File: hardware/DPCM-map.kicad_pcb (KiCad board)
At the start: 2 copper layers, 178 x 178 mm, 101 parts, among them J1 JMP, J2 Conn_01x06_Male, J3 Touch_Pad_+, J4 Touch_Pad_0, J5 Touch_Pad_-, J6 JMP, J7 Conn_01x06_Female, P1 USB_C_Plug, Q1 2N7002, Q2 2N7002, SW1 SW_Push, SW2 SW_+_Fb, SW3 SW_0_Fb, SW4 SW_-_Fb, U1 AZ1117-3.3, U2 BME280, U4 ESP32-WROOM-32, U5 CH340G, Y1 12MHz

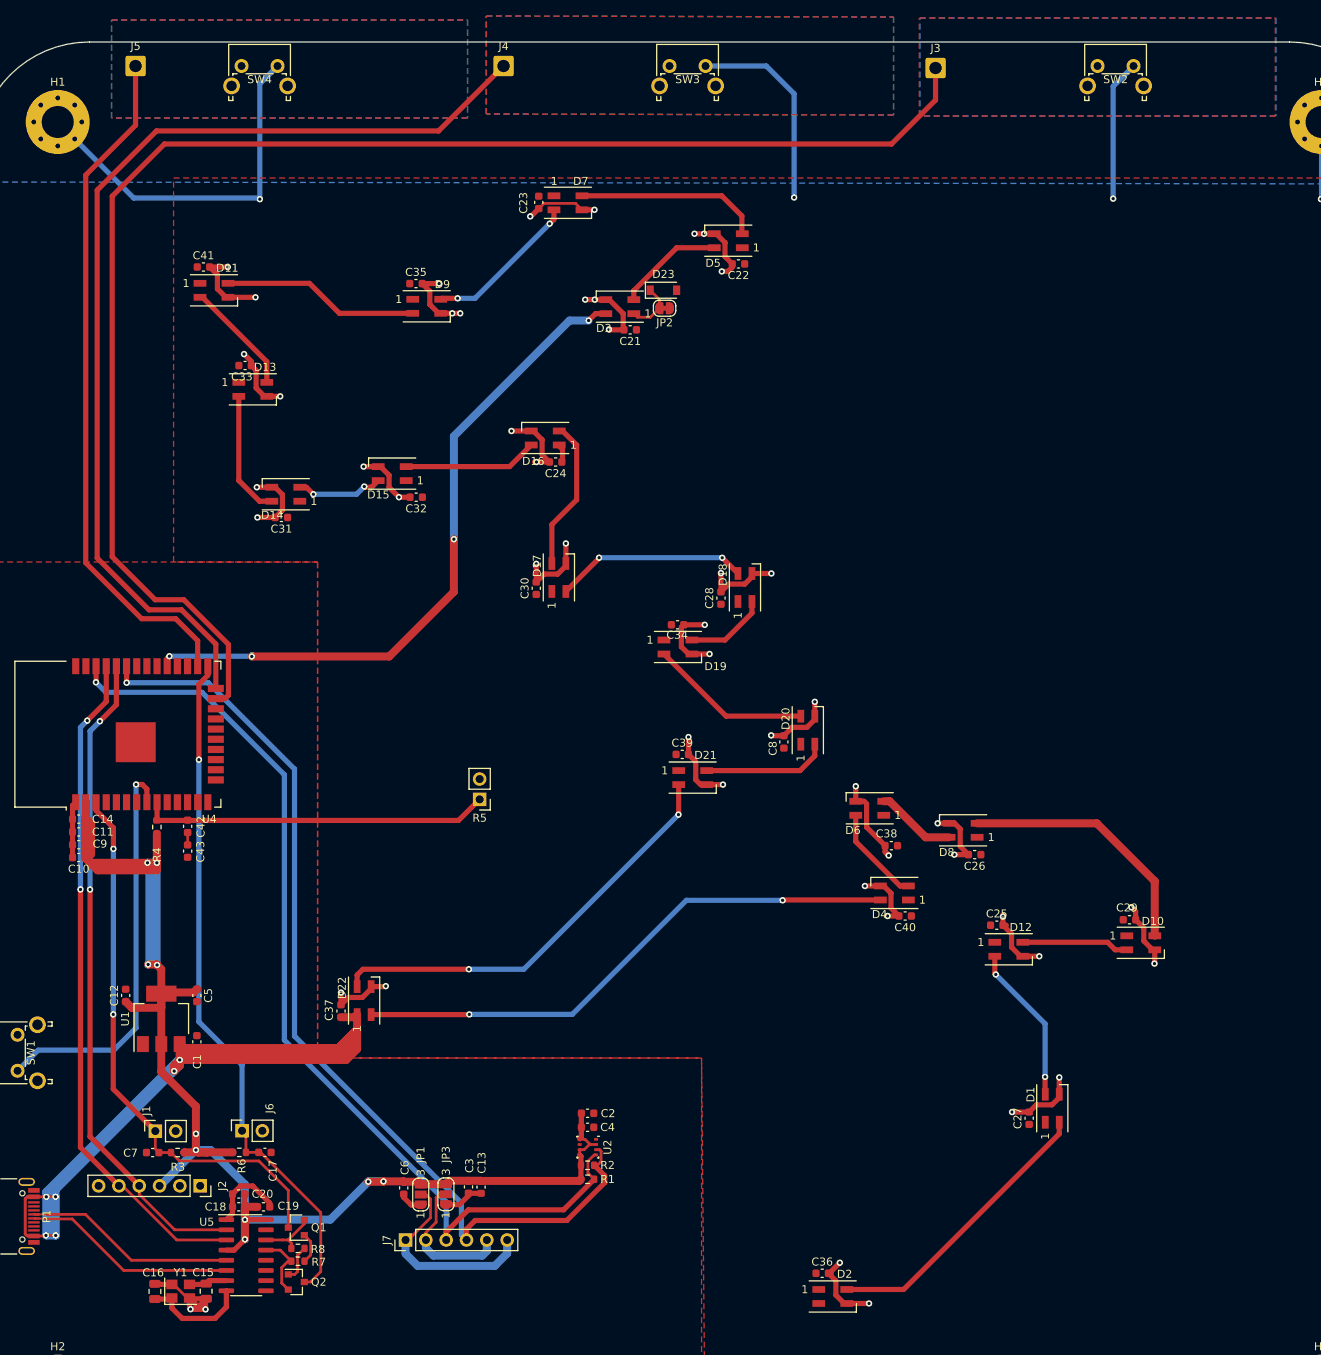
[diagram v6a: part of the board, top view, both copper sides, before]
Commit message: fix touchplates, optim traces and gnd fills
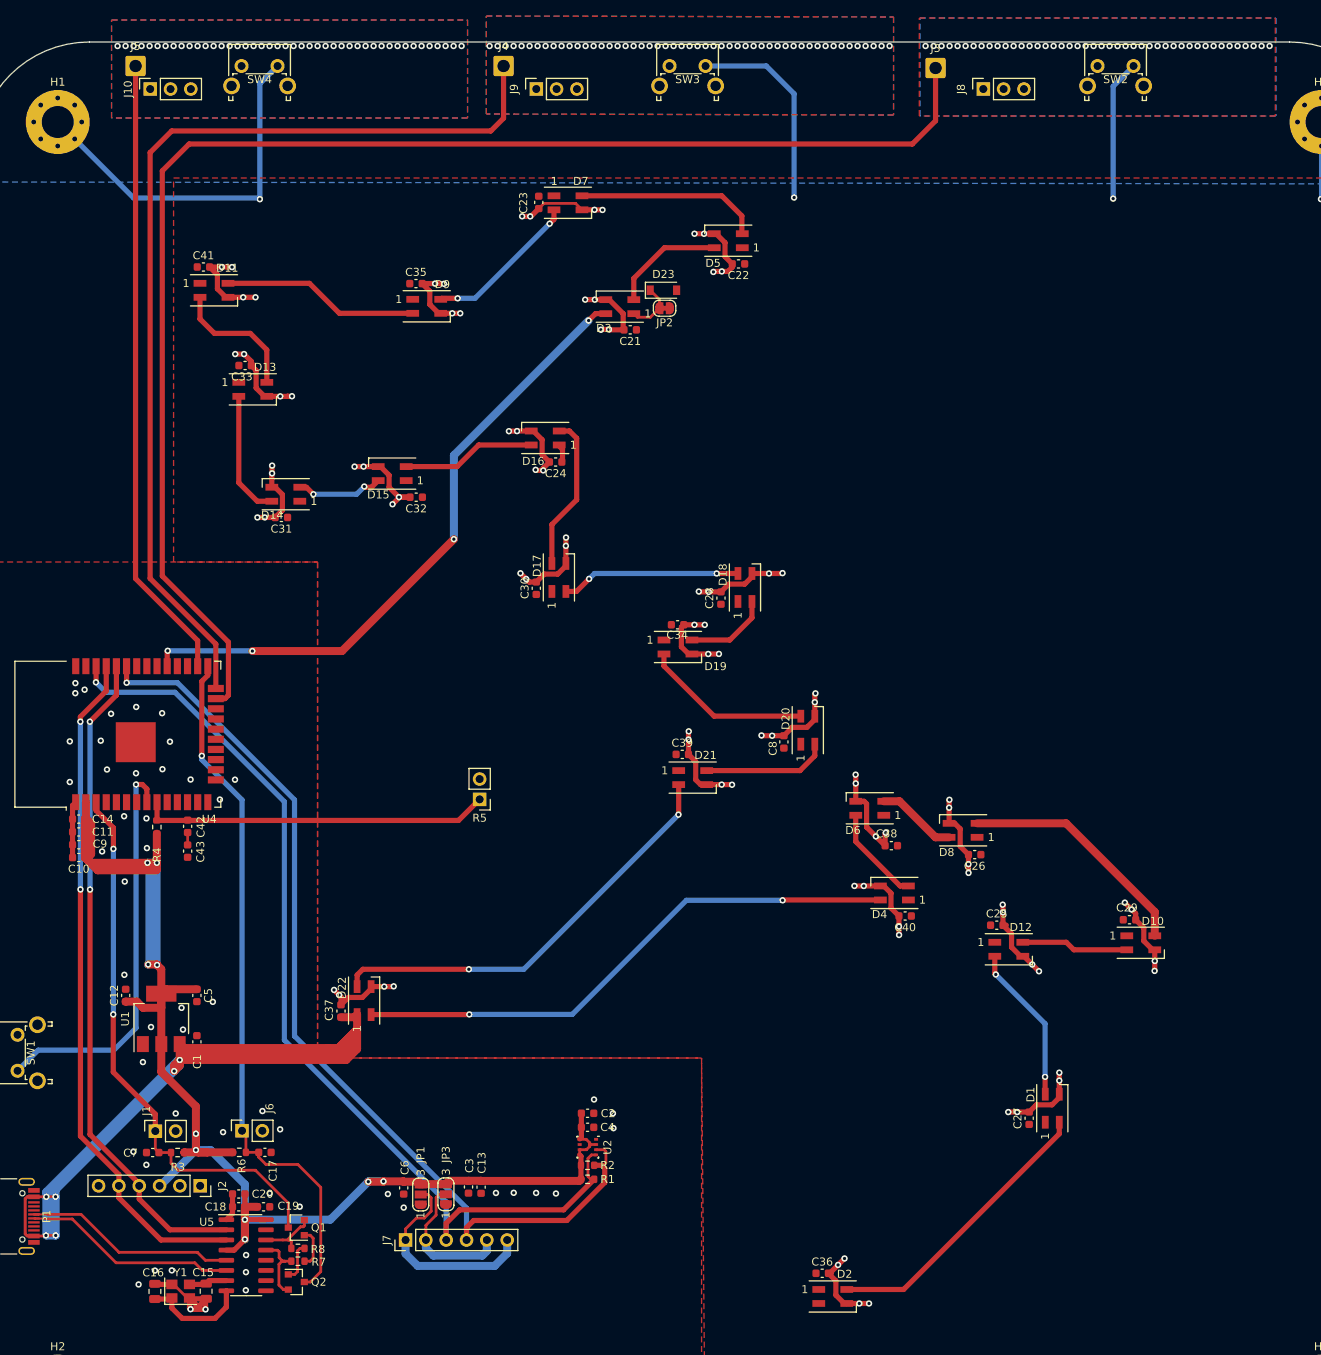
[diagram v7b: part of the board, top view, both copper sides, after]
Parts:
- added J10: Conn_01x03_Female, Connector_PinSocket_2.54mm:PinSocket_1x03_P2.54mm_Vertical, F.Cu at (132.1, 55.9)
- added J8: Conn_01x03_Female, Connector_PinSocket_2.54mm:PinSocket_1x03_P2.54mm_Vertical, F.Cu at (236.2, 55.9)
- added J9: Conn_01x03_Female, Connector_PinSocket_2.54mm:PinSocket_1x03_P2.54mm_Vertical, F.Cu at (180.3, 55.9)
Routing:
- net GND: track 348.5 -> 368.7 mm, vias 53 -> 144
- net TOUCH_-: track 85.9 -> 78.2 mm, vias 0 -> 44
- net TOUCH_+: track 184.1 -> 176.6 mm, vias 0 -> 44
- net TOUCH_0: track 128.0 -> 122.9 mm, vias 0 -> 51
- net LED_CHAIN: track 85.3 -> 80.3 mm
- net Net-(D11-Pad2): track 14.3 -> 16.7 mm
- net Net-(D10-Pad4): track 32.0 -> 29.8 mm
- net BOOT0: track 86.1 -> 88.0 mm
- net Net-(D17-Pad2): track 24.2 -> 22.4 mm
- net SDA: track 122.1 -> 120.8 mm
- net Net-(Q1-Pad1): track 3.90 -> 5.00 mm
- net Net-(D3-Pad2): track 13.4 -> 14.3 mm
- net TX: track 84.5 -> 85.4 mm
- net SCL: track 123.0 -> 122.2 mm
- net Net-(D19-Pad2): track 20.3 -> 21.2 mm
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
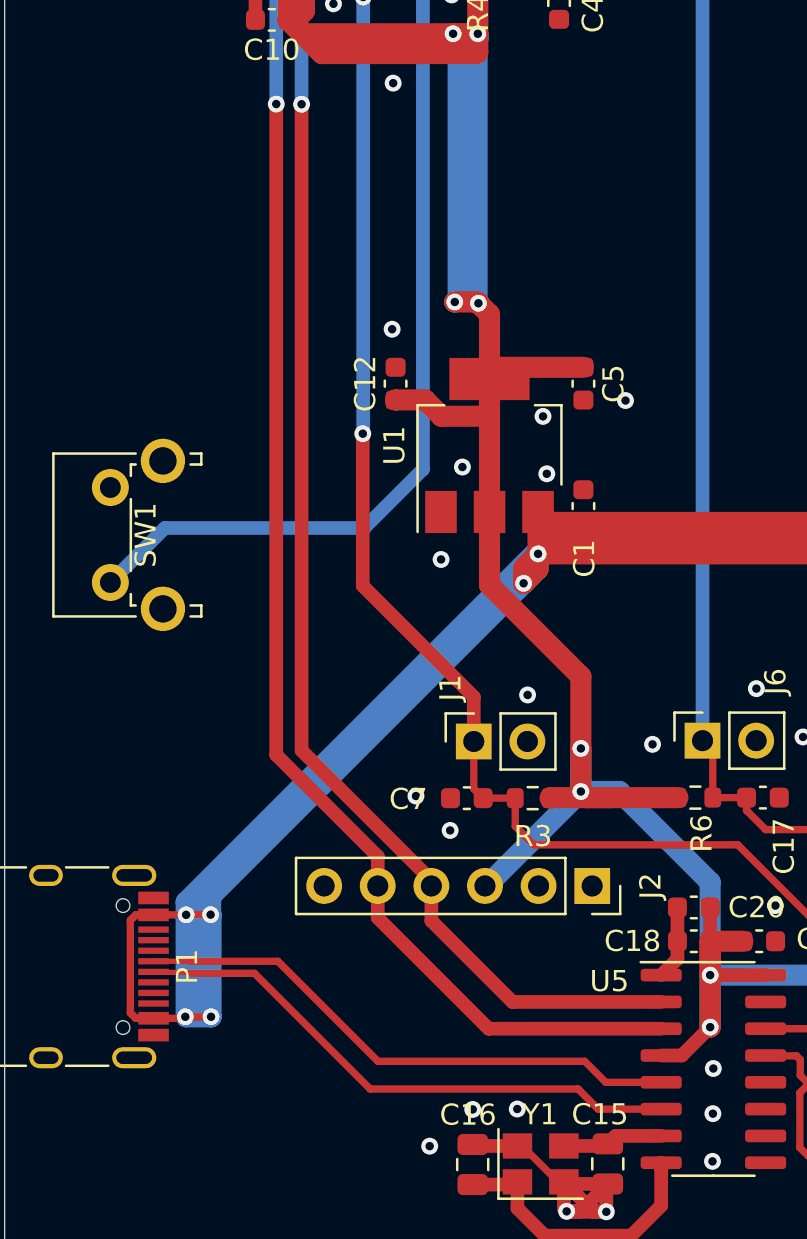
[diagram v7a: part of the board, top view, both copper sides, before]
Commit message: added heatsink for regulator
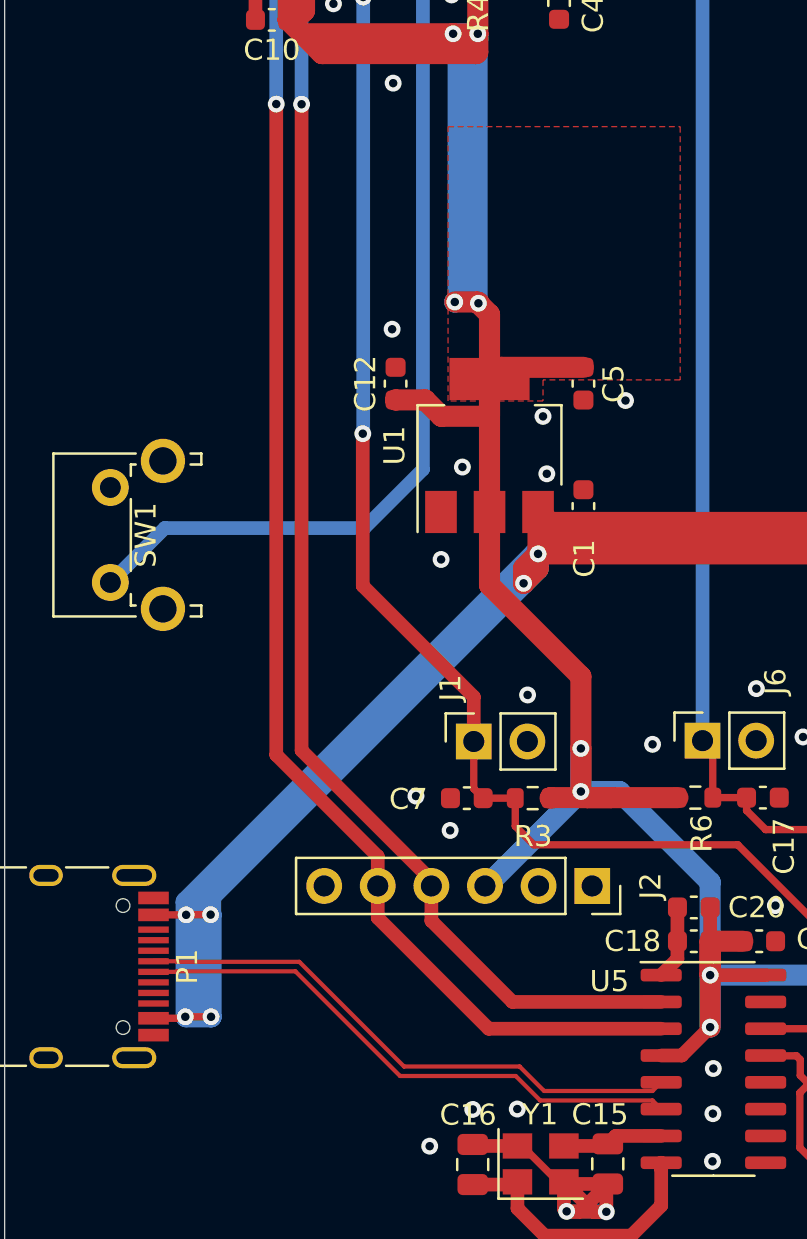
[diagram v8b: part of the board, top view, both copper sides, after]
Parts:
- C2: value 1u -> 10u
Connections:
- D2 pad 2: (no net) -> Net-(D2-Pad2)
- J2 pad 1: (no net) -> Net-(J2-Pad1)
- J2 pad 2: (no net) -> Net-(J2-Pad2)
- P1 pad A5: (no net) -> Net-(P1-PadA5)
- P1 pad A8: (no net) -> Net-(P1-PadA8)
- P1 pad B5: (no net) -> Net-(P1-PadB5)
- P1 pad B8: (no net) -> Net-(P1-PadB8)
- U4 pad 10: (no net) -> Net-(U4-Pad10)
- U4 pad 11: (no net) -> Net-(U4-Pad11)
- U4 pad 12: (no net) -> Net-(U4-Pad12)
- U4 pad 13: (no net) -> Net-(U4-Pad13)
- U4 pad 14: (no net) -> Net-(U4-Pad14)
- U4 pad 16: (no net) -> Net-(U4-Pad16)
- U4 pad 17: (no net) -> Net-(U4-Pad17)
- U4 pad 18: (no net) -> Net-(U4-Pad18)
- U4 pad 19: (no net) -> Net-(U4-Pad19)
- U4 pad 20: (no net) -> Net-(U4-Pad20)
- U4 pad 21: (no net) -> Net-(U4-Pad21)
- U4 pad 22: (no net) -> Net-(U4-Pad22)
- U4 pad 27: (no net) -> Net-(U4-Pad27)
- U4 pad 28: (no net) -> Net-(U4-Pad28)
- U4 pad 30: (no net) -> Net-(U4-Pad30)
- U4 pad 31: (no net) -> Net-(U4-Pad31)
- U4 pad 32: (no net) -> Net-(U4-Pad32)
- U4 pad 37: (no net) -> Net-(U4-Pad37)
- U4 pad 4: (no net) -> Net-(U4-Pad4)
- U4 pad 5: (no net) -> Net-(U4-Pad5)
- U4 pad 6: (no net) -> Net-(U4-Pad6)
- U4 pad 7: (no net) -> Net-(U4-Pad7)
- U5 pad 10: (no net) -> Net-(U5-Pad10)
- U5 pad 11: (no net) -> Net-(U5-Pad11)
- U5 pad 12: (no net) -> Net-(U5-Pad12)
- U5 pad 15: (no net) -> Net-(U5-Pad15)
- U5 pad 9: (no net) -> Net-(U5-Pad9)
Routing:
- net +5V: track 177.5 -> 164.0 mm
- added copper zone on F.Cu, net +3V3
